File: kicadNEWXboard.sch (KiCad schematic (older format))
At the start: 12 parts

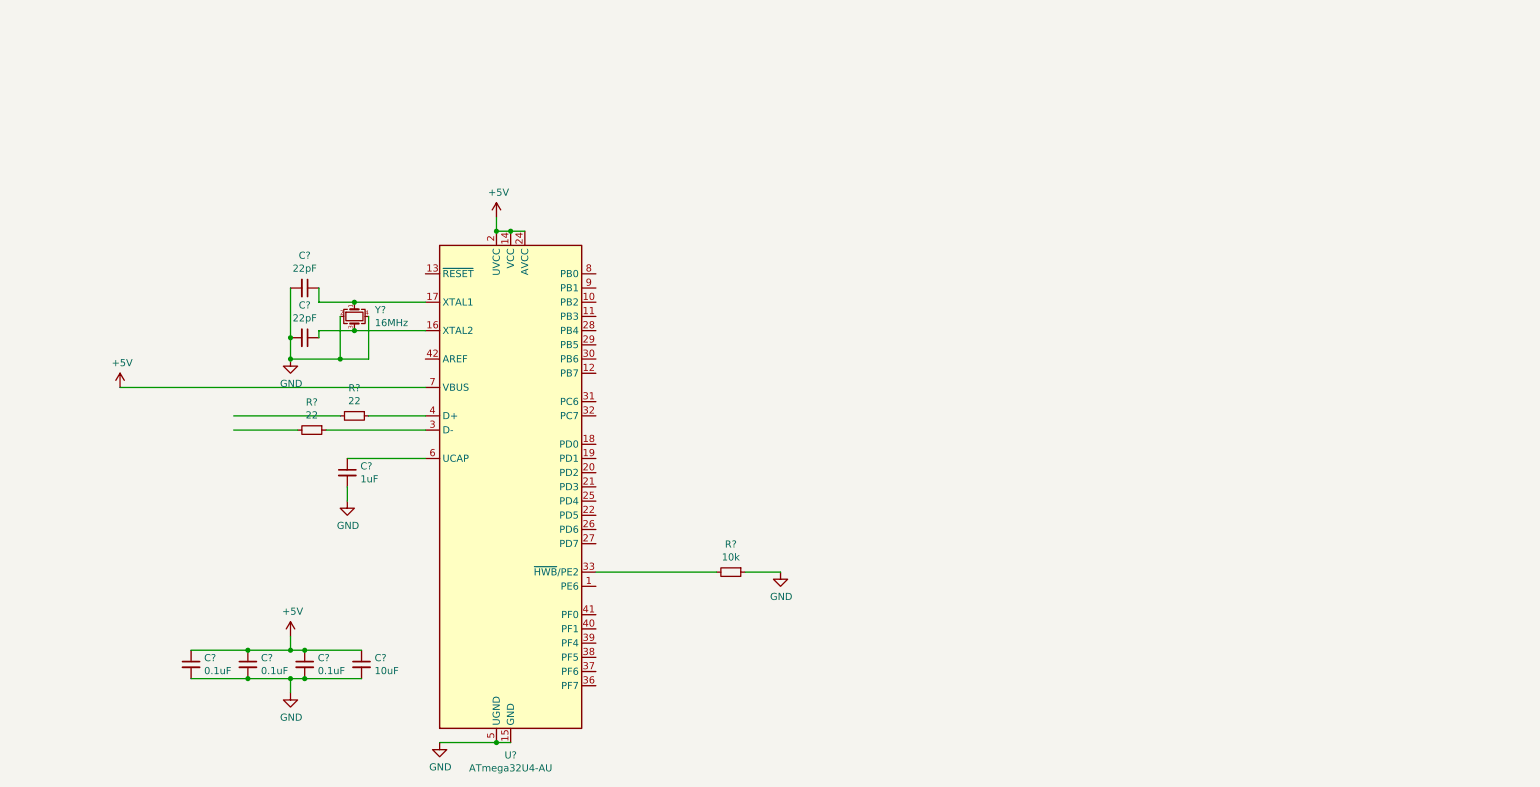
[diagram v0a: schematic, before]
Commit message: schematic and footprints bound
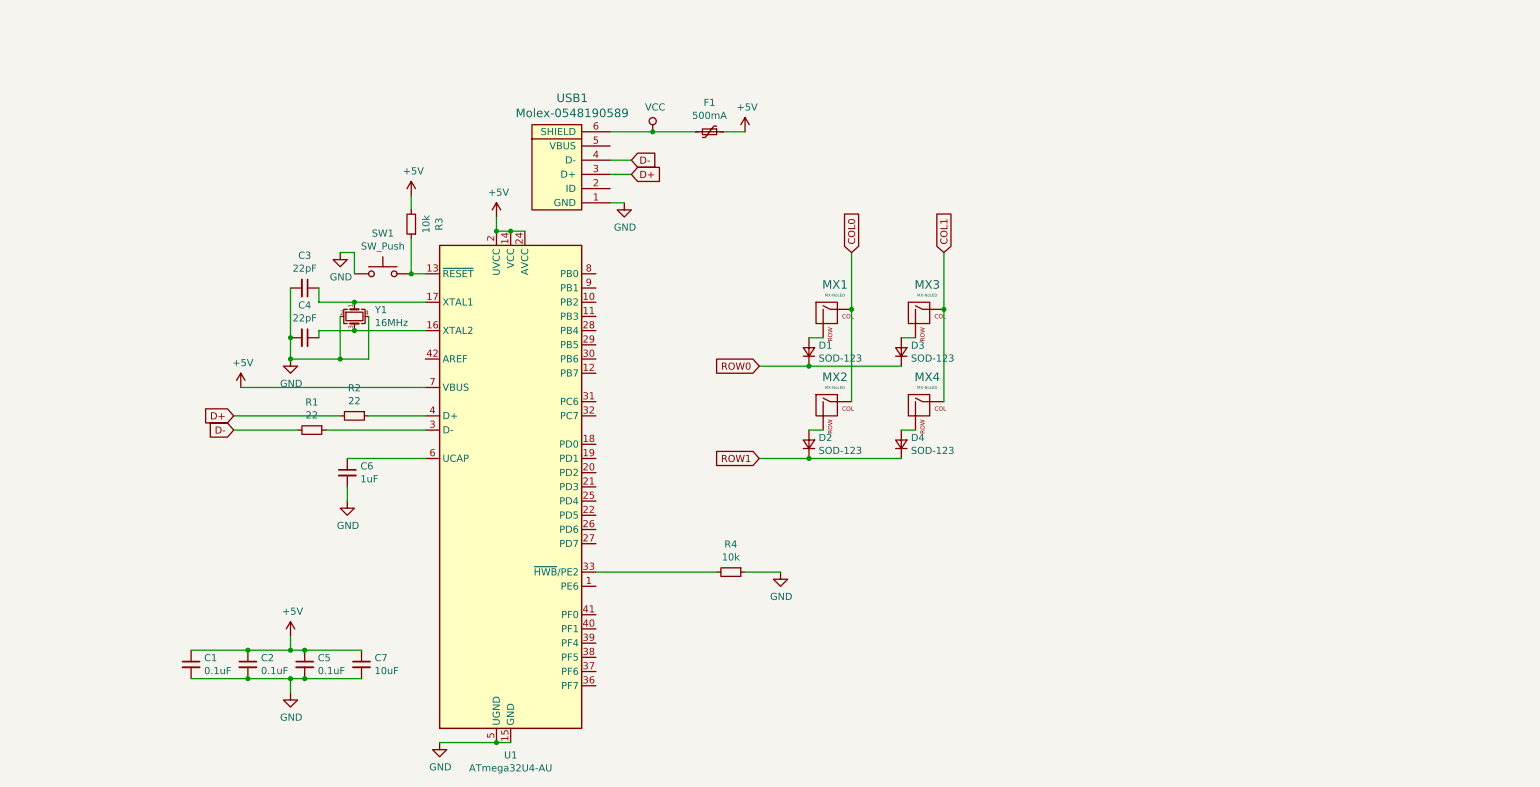
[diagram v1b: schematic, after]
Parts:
- added D1, D2, D3, D4: SOD-123, Diode_SMD:D_SOD-123, symbol Device:D_Small
- added F1: 500mA, Fuse:Fuse_1206_3216Metric, symbol Device:Polyfuse_Small
- added MX1, MX2, MX3, MX4: MX-NoLED, MX_Alps_Hybrid:MX-1U, symbol MX_Alps_Hybrid:MX-NoLED
- added R3: 10k, Resistor_SMD:R_0805_2012Metric, symbol Device:R_Small
- added SW1: SW_Push, random-keyboard-parts:SKQG-1155865, symbol Switch:SW_Push
- added USB1: Molex-0548190589, random-keyboard-parts:Molex-0548190519, symbol random-keyboard-parts:Molex-0548190589
- C1, C2, C3, C4, C5, C6, C7: renamed from C?; footprint (none) -> Capacitor_SMD:C_0805_2012Metric
- R1, R2, R4: renamed from R?; footprint (none) -> Resistor_SMD:R_0805_2012Metric
- Y1: renamed from Y?; footprint (none) -> Crystal:Crystal_SMD_3225-4Pin_3.2x2.5mm
- gave numbers to parts that had none: 1
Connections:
- net labels added: COL0, COL1, D+, D-, ROW0, ROW1, VCC
- wire segments 36 -> 59

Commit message: SVG
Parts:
- added D10, D11, D12, D13, D14, D15, D16, D17, D18, D19, D20, D21, D22, D23, D24, D25, D26, D27, D28, D29, D30, D31, D32, D33, D34, D35, D36, D37, D38, D39, D40, D41, D42, D43, D44, D45, D46, D47, D48, D5, D6, D7, D8, D9: SOD-123, Diode_SMD:D_SOD-123, symbol Device:D_Small
- added MX10, MX11, MX12, MX13, MX14, MX15, MX16, MX17, MX18, MX19, MX20, MX21, MX22, MX23, MX24, MX25, MX26, MX27, MX28, MX29, MX30, MX31, MX32, MX33, MX34, MX35, MX36, MX37, MX38, MX39, MX40, MX41, MX42, MX43, MX44, MX45, MX46, MX47, MX48, MX5, MX6, MX7, MX8, MX9: MX-NoLED, MX_Alps_Hybrid:MX-1U, symbol MX_Alps_Hybrid:MX-NoLED
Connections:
- net COL0: now also U1.18 (PD0), MX5.1 (COL), MX6.1 (COL), MX7.1 (COL)
- net COL1: now also U1.19 (PD1), MX10.1 (COL), MX8.1 (COL), MX9.1 (COL)
- net ROW0: now also U1.37 (PF6), D11.1 (K), D16.1 (K), D21.1 (K), D26.1 (K), D31.1 (K), D36.1 (K), D41.1 (K), D46.1 (K)
- net ROW1: now also U1.38 (PF5), D12.1 (K), D17.1 (K), D22.1 (K), D27.1 (K), D32.1 (K), D37.1 (K), D42.1 (K), D47.1 (K)
- net COL2: now reaches U1.20 (PD2)
- net COL2: now also MX11.1 (COL), MX12.1 (COL), MX13.1 (COL), MX14.1 (COL), MX15.1 (COL)
- net COL3: now reaches U1.21 (PD3)
- net COL3: now also MX16.1 (COL), MX17.1 (COL), MX18.1 (COL), MX19.1 (COL), MX20.1 (COL)
- net COL4: now reaches U1.22 (PD5)
- net COL4: now also MX21.1 (COL), MX22.1 (COL), MX23.1 (COL), MX24.1 (COL), MX25.1 (COL)
- net COL5: now reaches U1.26 (PD6)
- net COL5: now also MX26.1 (COL), MX27.1 (COL), MX28.1 (COL), MX29.1 (COL), MX30.1 (COL)
- net COL6: now reaches U1.27 (PD7)
- net COL6: now also MX31.1 (COL), MX32.1 (COL), MX33.1 (COL), MX34.1 (COL), MX35.1 (COL)
- net COL7: now reaches U1.28 (PB4)
- net COL7: now also MX36.1 (COL), MX37.1 (COL), MX38.1 (COL), MX39.1 (COL), MX40.1 (COL)
- net COL8: now reaches U1.29 (PB5)
- net COL8: now also MX41.1 (COL), MX42.1 (COL), MX43.1 (COL), MX44.1 (COL), MX45.1 (COL)
- net COL9: now reaches U1.30 (PB6)
- net COL9: now also MX46.1 (COL), MX47.1 (COL), MX48.1 (COL)
- net ROW2: now reaches U1.39 (PF4)
- net ROW2: now also D13.1 (K), D18.1 (K), D23.1 (K), D28.1 (K), D33.1 (K), D38.1 (K), D43.1 (K), D5.1 (K), D8.1 (K)
- net ROW3: now reaches U1.40 (PF1)
- net ROW3: now also D14.1 (K), D19.1 (K), D24.1 (K), D29.1 (K), D34.1 (K), D39.1 (K), D44.1 (K), D48.1 (K), D6.1 (K), D9.1 (K)
- net ROW4: now reaches U1.41 (PF0)
- net ROW4: now also D10.1 (K), D15.1 (K), D20.1 (K), D25.1 (K), D30.1 (K), D35.1 (K), D40.1 (K), D45.1 (K), D7.1 (K)
- new net: D17.2 (A), MX17.2 (ROW)
- new net: D12.2 (A), MX12.2 (ROW)
- new net: D16.2 (A), MX16.2 (ROW)
- new net: D11.2 (A), MX11.2 (ROW)
- new net: D27.2 (A), MX27.2 (ROW)
- new net: D22.2 (A), MX22.2 (ROW)
- new net: D26.2 (A), MX26.2 (ROW)
- new net: D21.2 (A), MX21.2 (ROW)
- new net: D37.2 (A), MX37.2 (ROW)
- new net: D32.2 (A), MX32.2 (ROW)
- new net: D36.2 (A), MX36.2 (ROW)
- new net: D31.2 (A), MX31.2 (ROW)
- new net: D47.2 (A), MX47.2 (ROW)
- new net: D42.2 (A), MX42.2 (ROW)
- new net: D46.2 (A), MX46.2 (ROW)
- new net: D41.2 (A), MX41.2 (ROW)
- new net: D9.2 (A), MX9.2 (ROW)
- new net: D6.2 (A), MX6.2 (ROW)
- new net: D8.2 (A), MX8.2 (ROW)
- new net: D5.2 (A), MX5.2 (ROW)
- new net: D19.2 (A), MX19.2 (ROW)
- new net: D14.2 (A), MX14.2 (ROW)
- new net: D18.2 (A), MX18.2 (ROW)
- new net: D13.2 (A), MX13.2 (ROW)
- new net: D29.2 (A), MX29.2 (ROW)
- new net: D24.2 (A), MX24.2 (ROW)
- new net: D28.2 (A), MX28.2 (ROW)
- new net: D23.2 (A), MX23.2 (ROW)
- new net: D39.2 (A), MX39.2 (ROW)
- new net: D34.2 (A), MX34.2 (ROW)
- new net: D38.2 (A), MX38.2 (ROW)
- new net: D33.2 (A), MX33.2 (ROW)
- new net: D48.2 (A), MX48.2 (ROW)
- new net: D44.2 (A), MX44.2 (ROW)
- new net: D43.2 (A), MX43.2 (ROW)
- new net: D10.2 (A), MX10.2 (ROW)
- new net: D7.2 (A), MX7.2 (ROW)
- new net: D20.2 (A), MX20.2 (ROW)
- new net: D15.2 (A), MX15.2 (ROW)
- new net: D30.2 (A), MX30.2 (ROW)
- new net: D25.2 (A), MX25.2 (ROW)
- new net: D40.2 (A), MX40.2 (ROW)
- new net: D35.2 (A), MX35.2 (ROW)
- new net: D45.2 (A), MX45.2 (ROW)
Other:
- moved on the sheet: C1, C2, C3, C4, C5, C6, C7, D1, D2, D3, D4, F1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
